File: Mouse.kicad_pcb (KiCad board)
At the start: 2 copper layers, 39 x 78 mm, 27 parts, among them J1 Conn_01x05_Male, U1 Left click, U2 Middle click, U3 Right Click, U4 LQ1, U5 Optical_Sensor

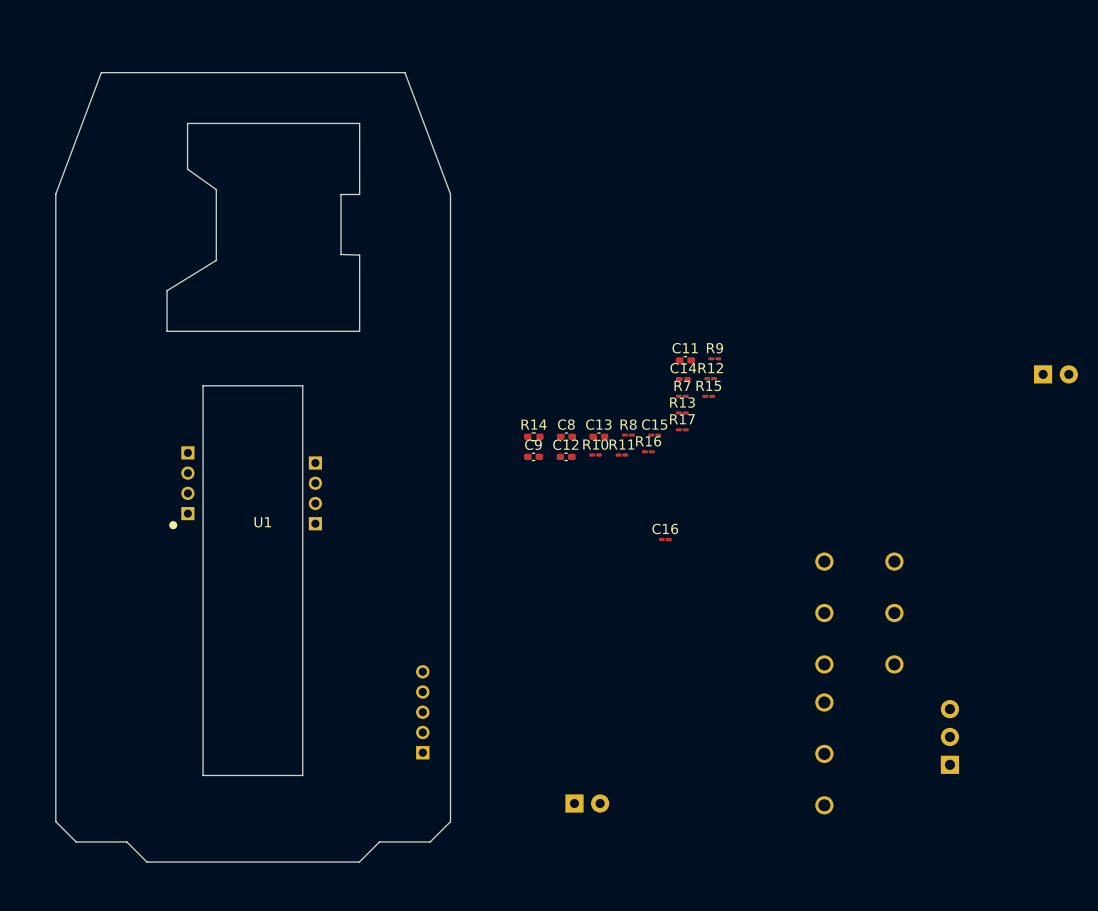
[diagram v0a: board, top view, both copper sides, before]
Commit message: Updated layout
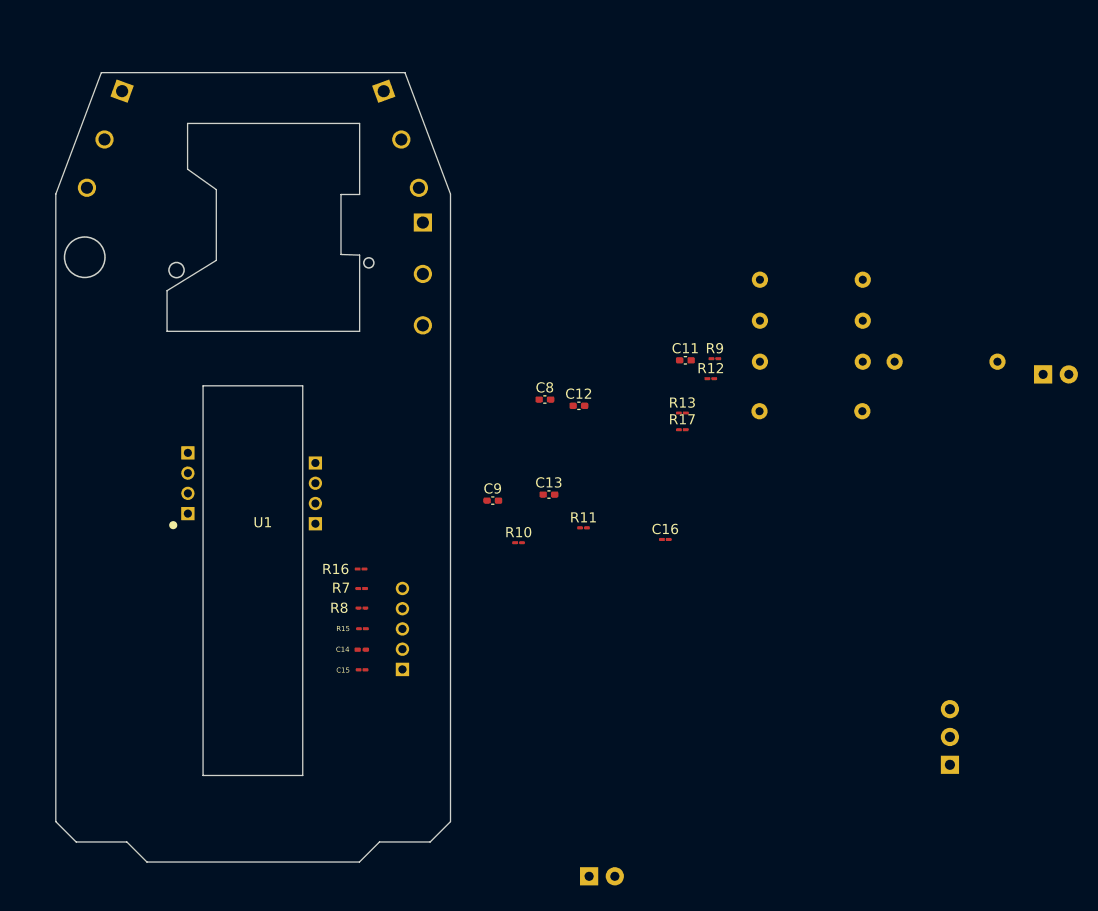
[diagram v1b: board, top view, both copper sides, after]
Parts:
- added JP1: R, Resistor_THT:R_Axial_DIN0207_L6.3mm_D2.5mm_P10.16mm_Horizontal, B.Cu at (146.7, 103.4)
- added JP2: R, Resistor_THT:R_Axial_DIN0207_L6.3mm_D2.5mm_P10.16mm_Horizontal, B.Cu at (146.7, 99.4)
- added JP3: R, Resistor_THT:R_Axial_DIN0207_L6.3mm_D2.5mm_P10.16mm_Horizontal, B.Cu at (160.0, 103.4)
- added JP4: R, Resistor_THT:R_Axial_DIN0207_L6.3mm_D2.5mm_P10.16mm_Horizontal, B.Cu at (146.7, 95.3)
- R14: footprint Resistor_SMD:R_0402_1005Metric_Pad0.72x0.64mm_HandSolder -> Resistor_THT:R_Axial_DIN0207_L6.3mm_D2.5mm_P10.16mm_Horizontal; moved to B.Cu
- moved U3 91.0 mm to (82.0, 81.5), turned to 160 degrees
- moved U1 62.7 mm to (111.3, 81.5), turned to 200 degrees
- moved U2 61.8 mm to (113.4, 94.7), turned to 180 degrees
- moved C14 41.5 mm to (107.4, 131.9), turned to 180 degrees
- moved R15 41.2 mm to (107.4, 129.8)
- moved C15 37.1 mm to (107.4, 133.9)
- moved R7 36.9 mm to (107.4, 125.8), turned to 180 degrees
- moved R8 31.4 mm to (107.4, 127.8)
- moved R16 30.7 mm to (107.3, 123.9)
- moved R14 22.4 mm to (146.7, 108.3)
- moved R10 11.5 mm to (122.9, 121.3)
- moved J1 8.47 mm to (111.4, 129.8)
- moved R11 8.13 mm to (129.3, 119.8)
- moved LD2 7.34 mm to (129.8, 154.3)
- moved C9 5.91 mm to (120.3, 117.1)
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- renumbered C13 to C12, C12 to C13
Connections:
- C16 pad 1: Pin_2 -> Net-(C16-Pad1)
- LD1 pad 2: Pin_2 -> Net-(C16-Pad1)
- LD2 pad 2: Pin_1 -> Net-(JP3-Pad1)
- R11 pad 2: Net-(R11-Pad2) -> Net-(JP2-Pad2)
- R16 pad 1: Pin_2 -> Net-(JP4-Pad1)
- U2 pad 1: Net-(R11-Pad2) -> Net-(JP2-Pad1)
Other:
- outline, holes or cut-outs redrawn

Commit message: Updated board layout
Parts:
- C11, C12, C13, C8, C9: footprint Capacitor_SMD:C_0402_1005Metric_Pad0.74x0.62mm_HandSolder -> Mouse:R_0603_1608_Logi
- C14: footprint Capacitor_SMD:C_0201_0603Metric_Pad0.64x0.40mm_HandSolder -> Mouse:R_0603_1608_Logi
- C15, C16: footprint Capacitor_SMD:C_01005_0402Metric_Pad0.57x0.30mm_HandSolder -> Mouse:R_0603_1608_Logi
- JP1, JP2, JP3, JP4, R14: footprint Resistor_THT:R_Axial_DIN0207_L6.3mm_D2.5mm_P10.16mm_Horizontal -> Mouse:JP_Axial_DIN0207_L6.3mm_D2.5mm_P10.16mm_Horizontal
- LD1: footprint LED_THT:LED_D2.0mm_W4.0mm_H2.8mm_FlatTop -> Mouse:Rot_LED
- LD2: footprint LED_THT:LED_D5.0mm_Horizontal_O6.35mm_Z15.0mm -> Mouse:LED_Sensor
- R10, R11, R12, R13, R15, R16, R17, R7, R8, R9: footprint Resistor_SMD:R_01005_0402Metric_Pad0.57x0.30mm_HandSolder -> Mouse:R_0603_1608_Logi
- moved U4 90.2 mm to (91.1, 89.5), turned to 180 degrees
- moved JP3 79.4 mm to (87.1, 134.9), turned to 90 degrees
- moved JP2 68.2 mm to (82.3, 121.6), turned to 95 degrees
- moved LD1 66.4 mm to (110.1, 89.5), turned to 270 degrees
- moved R14 61.1 mm to (85.7, 112.8), turned to 115 degrees
- moved JP1 56.1 mm to (90.7, 105.3), turned to 20 degrees
- moved R17 53.5 mm to (86.4, 119.9)
- moved JP4 49.4 mm to (105.5, 122.6), turned to 90 degrees
- moved C12 43.3 mm to (86.4, 116.4)
- moved R11 42.9 mm to (86.4, 121.6), turned to 180 degrees
- moved C13 39.5 mm to (86.4, 118.2)
- moved C16 37.0 mm to (108.7, 97.5)
- moved R12 34.6 mm to (108.7, 114.8)
- moved R9 33.6 mm to (108.8, 105.1)
- moved LD2 33.3 mm to (96.8, 150.3), turned to 180 degrees
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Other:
- outline, holes or cut-outs redrawn

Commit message: Layout Updated
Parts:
- moved JP2 10.8 mm to (81.8, 110.8), turned to 275 degrees
- moved R14 10.4 mm to (82.5, 102.9), turned to 285 degrees
- moved JP1 10.2 mm to (100.2, 101.8), turned to 200 degrees
- moved LQ1 1.08 mm to (90.1, 89.5)
- moved LD1 1.05 mm to (109.0, 89.5)
- moved C16 1.01 mm to (108.4, 96.6), turned to 180 degrees
- moved R9 0.89 mm to (108.8, 106.0), turned to 180 degrees
- moved R10 0.89 mm to (108.7, 107.7)
- moved R13 0.89 mm to (108.7, 109.3), turned to 180 degrees
- moved JP4 0.76 mm to (105.5, 121.8)
- moved C8 0.38 mm to (108.7, 120.8)
- moved R16 0.28 mm to (108.7, 123.6), turned to 180 degrees
- moved SW1 0.24 mm to (111.1, 81.4)
- moved SW3 0.20 mm to (113.4, 94.0)
- moved SW2 0.19 mm to (82.2, 81.4)
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- renumbered U4 to LQ1, U1 to SW1, U3 to SW2, U2 to SW3, U5 to U1
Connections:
- C16 pad 1: Net-(C16-Pad1) -> Pin_2J
- JP1 pad 1: Net-(C16-Pad1) -> Pin_2J
- LD1 pad 2: Net-(C16-Pad1) -> Pin_2J
- LD2 pad 1: Net-(LD2-Pad1) -> Net-(JP3-Pad1)
- LD2 pad 2: Net-(JP3-Pad1) -> Net-(LD2-Pad2)
- LQ1 pad 2: Pin_2 -> Pin_2J
- R12 pad 2: Net-(LD2-Pad1) -> Net-(LD2-Pad2)
- SW1 pad 2: Pin_2 -> Pin_2J
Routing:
- net Pin_4: track 0.00 -> 98.7 mm
- net Net-(R9-Pad2): track 0.00 -> 91.0 mm
- net Net-(R10-Pad1): track 0.00 -> 69.4 mm
- net Pin_2J: track 0.00 -> 66.2 mm
- net Net-(LD1-Pad1): track 0.00 -> 61.3 mm
- net Net-(LD2-Pad2): track 0.00 -> 48.8 mm
- net Net-(JP2-Pad1): track 0.00 -> 46.2 mm
- net Pin_2: track 0.00 -> 43.6 mm
- net Net-(JP3-Pad1): track 0.00 -> 22.1 mm
- net D+: track 0.00 -> 17.9 mm
- net Pin_5: track 0.00 -> 14.7 mm
- net D-: track 0.00 -> 13.0 mm
- net Net-(C14-Pad2): track 0.00 -> 11.6 mm
- net Pin_1: track 0.00 -> 6.93 mm
- net Pin_3: track 0.00 -> 6.35 mm
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- added copper zone on F.Cu, net GNDREF
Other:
- outline, holes or cut-outs redrawn

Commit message: Updated Schematics, Layout and Footprints
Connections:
- R7 pad 1: D- -> Pin_8
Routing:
- net D-: track 13.0 -> 0.00 mm
- net Pin_8: track 0.00 -> 13.0 mm
- net Net-(JP2-Pad1): track 46.2 -> 49.4 mm
- net GNDREF: track 1.90 -> 3.29 mm
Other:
- board text added: "01 6C"
- board text added: "210-001515 Rev. 001"
- board text added: "94V-0"
- board text added: "E301791"
- board text added: "Mouton 1D CR"
- board text added: "SWZ-2"
- board text added: "github.com/RandomDelta6"
